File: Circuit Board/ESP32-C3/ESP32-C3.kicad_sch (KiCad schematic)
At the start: 41 parts

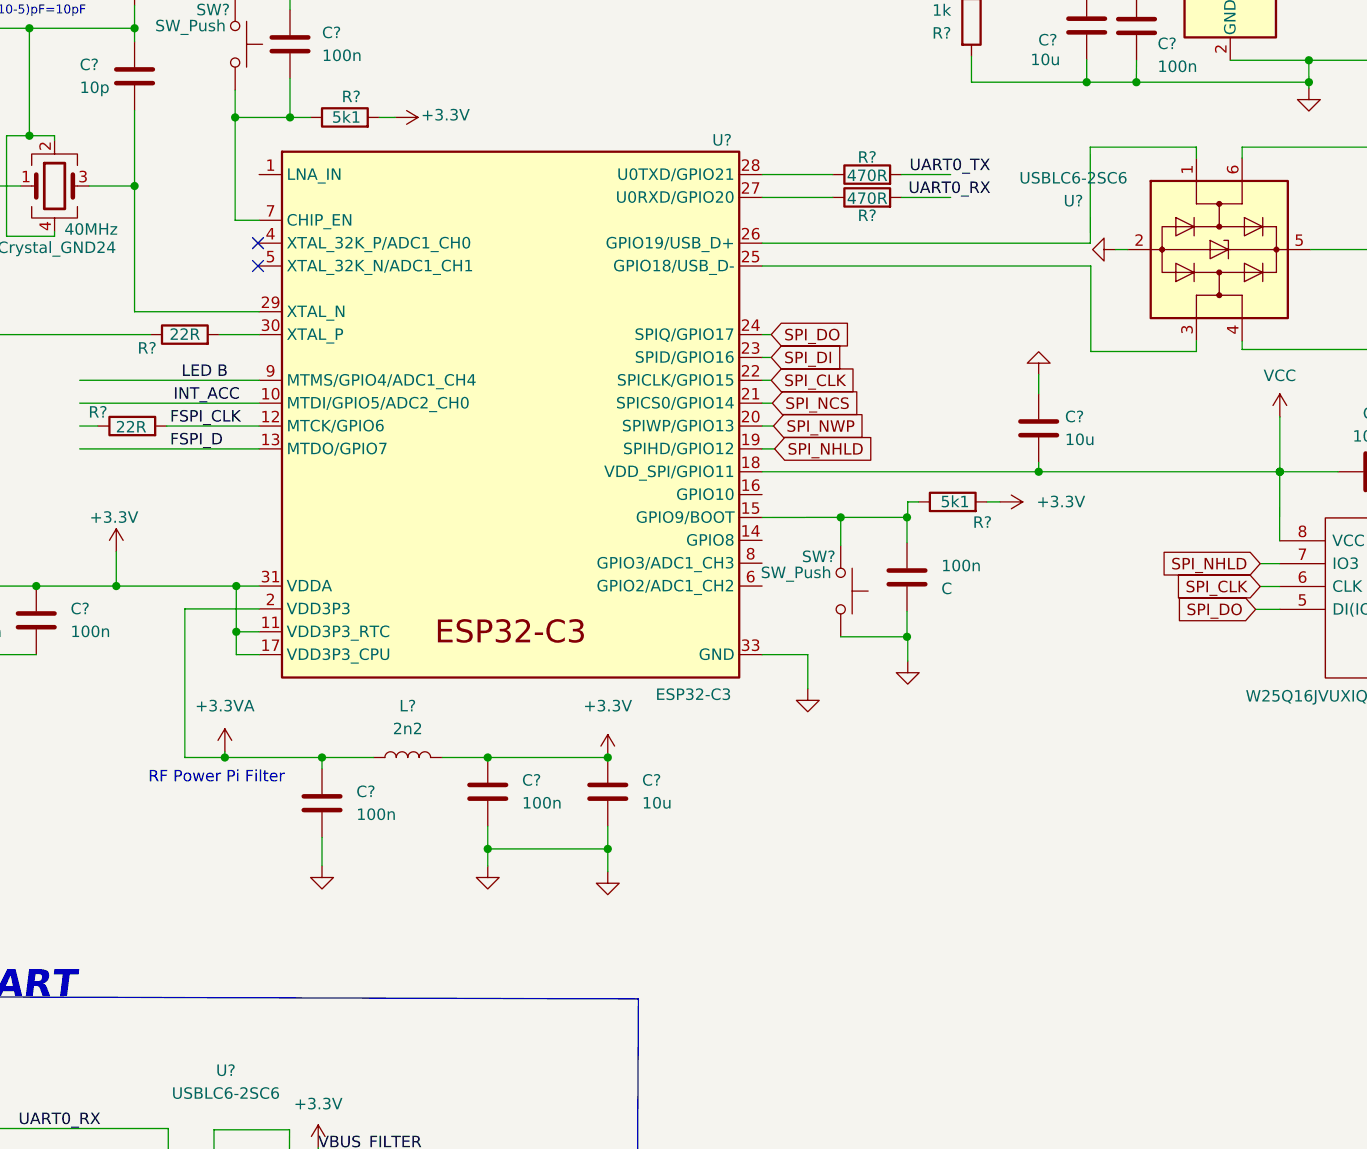
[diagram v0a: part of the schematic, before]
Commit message: Added RF antenna circuit
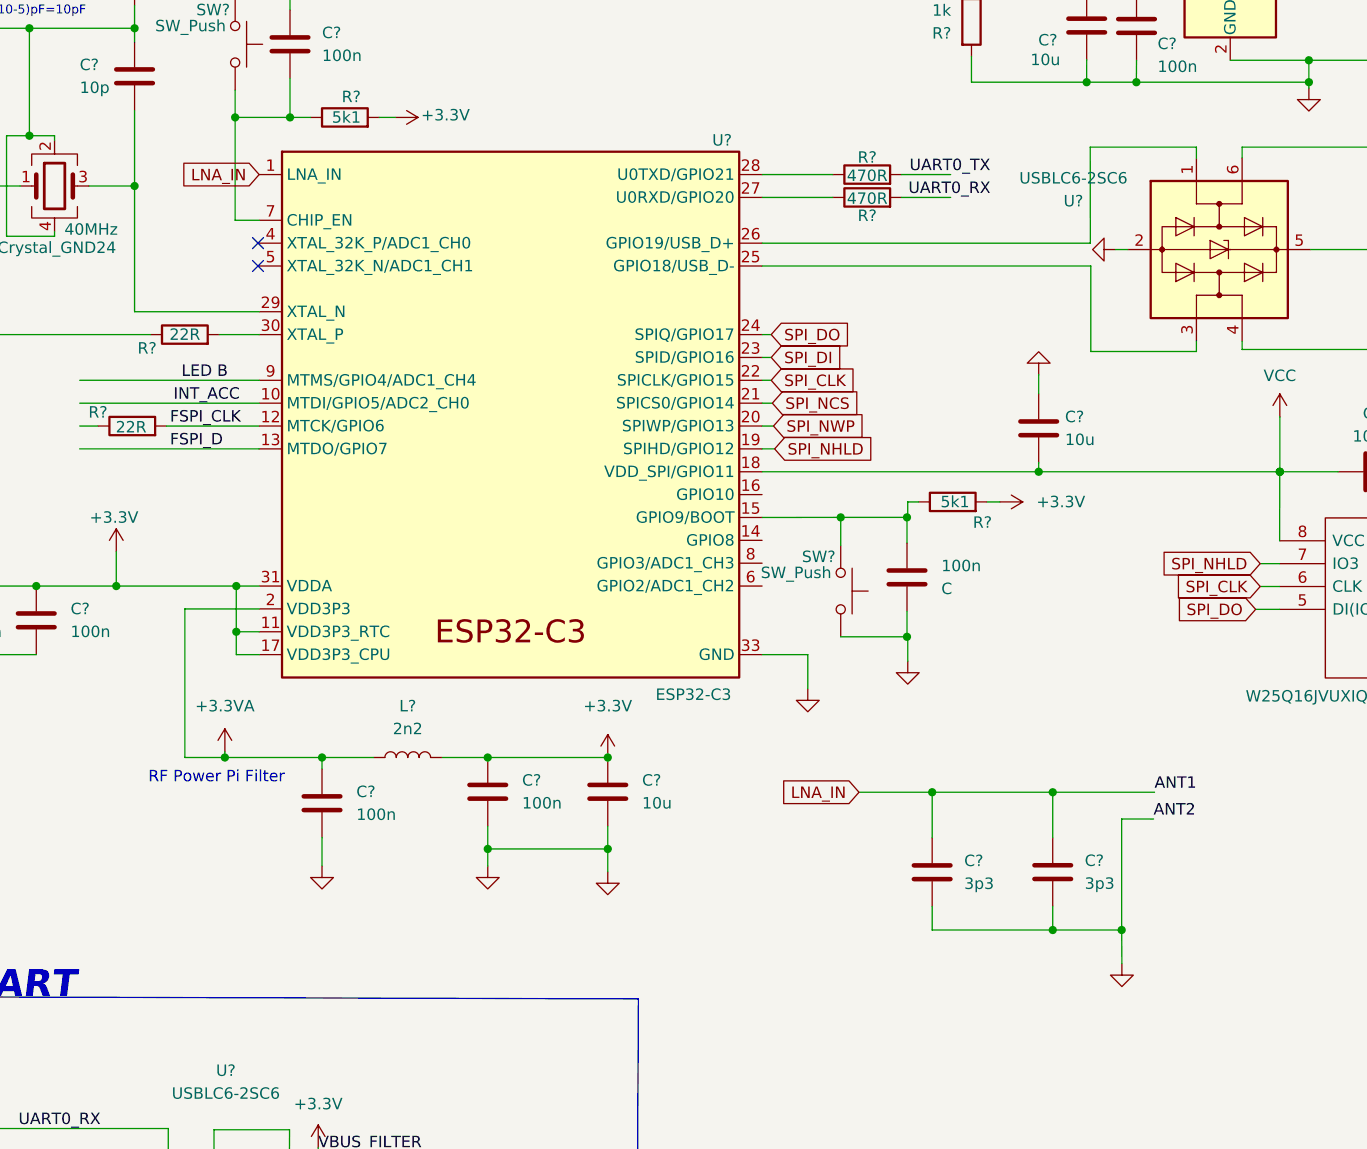
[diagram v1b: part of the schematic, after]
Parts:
- added C? (x2): 3p3, symbol Device:C
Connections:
- net +3.3V: now also C?.2, C?.2
- net LNA_IN: now reaches U?.1 (LNA_IN)
- net LNA_IN: now also C?.1, C?.1
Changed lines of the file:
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@@
   (junction (at 119.1514 120.5992) (diameter 0) (color 0 0 0 0)
   )
+  (junction (at 155.194 114.3) (diameter 0) (color 0 0 0 0)
+  )
   (junction (at 77.8764 96.4692) (diameter 0) (color 0 0 0 0)
   )
+  (junction (at 168.5923 114.2998) (diameter 0) (color 0 0 0 0)
+  )
   (junction (at 193.8274 78.6892) (diameter 0) (color 0 0 0 0)
   )
@@
   (junction (at 77.8764 91.3892) (diameter 0) (color 0 0 0 0)
   )
+  (junction (at 176.2524 129.6082) (diameter 0) (color 0 0 0 0)
+  )
   (junction (at 87.4014 110.4392) (diameter 0) (color 0 0 0 0)
   )
@@
   )
   (junction (at 145.034 83.7593) (diameter 0) (color 0 0 0 0)
+  )
+  (junction (at 168.5923 129.6082) (diameter 0) (color 0 0 0 0)
   )
   (junction (at 177.8846 35.4076) (diameter 0) (color 0 0 0 0)
@@
     (stroke (width 0) (type default) (color 0 0 0 0))
   )
+  (wire (pts (xy 155.194 127) (xy 155.194 129.6082))
+    (stroke (width 0) (type default) (color 0 0 0 0))
+  )
   (wire (pts (xy 75.3991 154.044) (xy 75.3991 151.802))
     (stroke (width 0) (type default) (color 0 0 0 0))
@@
     (stroke (width 0) (type default) (color 0 0 0 0))
   )
+  (wire (pts (xy 168.5923 114.2998) (xy 168.5923 119.3656))
+    (stroke (width 0) (type default) (color 0 0 0 0))
+  )
   (wire (pts (xy 159.5628 22.8057) (xy 159.5628 24.892))
     (stroke (width 0) (type default) (color 0 0 0 0))
@@
     (stroke (width 0) (type default) (color 0 0 0 0))
   )
+  (wire (pts (xy 147.066 114.3) (xy 155.194 114.3))
+    (stroke (width 0) (type default) (color 0 0 0 0))
+  )
   (wire (pts (xy 152.484 97.028) (xy 152.484 99.748))
     (stroke (width 0) (type default) (color 0 0 0 0))
@@
     (stroke (width 0) (type default) (color 0 0 0 0))
   )
+  (wire (pts (xy 155.194 114.3) (xy 168.5923 114.2998))
+    (stroke (width 0) (type default) (color 0 0 0 0))
+  )
   (wire (pts (xy 255.8542 77.3684) (xy 255.8796 73.4568))
     (stroke (width 0) (type default) (color 0 0 0 0))
@@
     (stroke (width 0) (type default) (color 0 0 0 0))
   )
+  (wire (pts (xy 168.5923 129.6082) (xy 176.2524 129.6082))
+    (stroke (width 0) (type default) (color 0 0 0 0))
+  )
   (wire (pts (xy 66.5734 46.9392) (xy 66.5734 60.9092))
     (stroke (width 0) (type default) (color 0 0 0 0))
@@
     (stroke (width 0) (type default) (color 0 0 0 0))
   )
+  (wire (pts (xy 168.5923 129.6082) (xy 168.5923 126.9856))
+    (stroke (width 0) (type default) (color 0 0 0 0))
+  )
+  (wire (pts (xy 155.194 114.3) (xy 155.194 119.38))
+    (stroke (width 0) (type default) (color 0 0 0 0))
+  )
   (wire (pts (xy 75.3991 174.364) (xy 75.3991 177.0155))
     (stroke (width 0) (type default) (color 0 0 0 0))
@@
     (stroke (width 0) (type default) (color 0 0 0 0))
   )
+  (wire (pts (xy 176.2524 117.2715) (xy 179.7925 117.2763))
+    (stroke (width 0) (type default) (color 0 0 0 0))
+  )
   (wire (pts (xy 45.7454 30.6832) (xy 45.7454 29.4132))
     (stroke (width 0) (type default) (color 0 0 0 0))
@@
     (stroke (width 0) (type default) (color 0 0 0 0))
   )
+  (wire (pts (xy 176.2524 129.6082) (xy 176.2524 117.2715))
+    (stroke (width 0) (type default) (color 0 0 0 0))
+  )
   (wire (pts (xy 167.0304 78.6892) (xy 167.0304 77.6732))
     (stroke (width 0) (type default) (color 0 0 0 0))
@@
     (stroke (width 0) (type default) (color 0 0 0 0))
   )
+  (wire (pts (xy 168.5923 114.2998) (xy 179.9008 114.2998))
+    (stroke (width 0) (type default) (color 0 0 0 0))
+  )
   (wire (pts (xy 223.6216 40.4368) (xy 218.4633 40.4368))
     (stroke (width 0) (type default) (color 0 0 0 0))
@@
     (stroke (width 0) (type default) (color 0 0 0 0))
   )
+  (wire (pts (xy 176.276 133.35) (xy 176.2524 129.6082))
+    (stroke (width 0) (type default) (color 0 0 0 0))
+  )
   (wire (pts (xy 197.998 22.8092) (xy 206.248 22.8092))
+    (stroke (width 0) (type default) (color 0 0 0 0))
+  )
+  (wire (pts (xy 155.194 129.6082) (xy 168.5923 129.6082))
     (stroke (width 0) (type default) (color 0 0 0 0))
   )
@@
     (effects (font (size 1 1)) (justify left bottom))
   )
+  (label "ANT1" (at 179.9008 114.2998 0)
+    (effects (font (size 1.27 1.27)) (justify left bottom))
+  )
   (label "LED B" (at 71.7804 68.5292 0)
     (effects (font (size 1.27 1.27)) (justify left bottom))
@@
   )
   (label "VBUS_FILTER" (at 86.9797 154.2376 0)
+    (effects (font (size 1.27 1.27)) (justify left bottom))
+  )
+  (label "ANT2" (at 179.7925 117.2763 0)
     (effects (font (size 1.27 1.27)) (justify left bottom))
   )
@@
     (effects (font (size 1.27 1.27)) (justify right))
     (property "Intersheet References" "${INTERSHEET_REFS}" (id 0) (at 181.6099 91.3606 0)
+      (effects (font (size 1.27 1.27)) (justify right) hide)
+    )
+  )
+  (global_label "LNA_IN" (shape input) (at 80.4164 45.6692 180) (fields_autoplaced)
+    (effects (font (size 1.27 1.27)) (justify right))
+    (property "Intersheet References" "${INTERSHEET_REFS}" (id 0) (at 71.6533 45.5898 0)
+      (effects (font (size 1.27 1.27)) (justify right) hide)
+    )
+  )
+  (global_label "LNA_IN" (shape input) (at 147.066 114.3 180) (fields_autoplaced)
+    (effects (font (size 1.27 1.27)) (justify right))
+    (property "Intersheet References" "${INTERSHEET_REFS}" (id 0) (at 138.3029 114.2206 0)
       (effects (font (size 1.27 1.27)) (justify right) hide)
     )
@@
     (pin "2")
   )
+  (symbol (lib_id "Device:C") (at 155.194 123.19 0) (unit 1)
+    (in_bom yes) (on_board yes) (fields_autoplaced)
+    (property "Reference" "C?" (id 0) (at 158.75 121.9199 0)
+      (effects (font (size 1.27 1.27)) (justify left))
+    )
+    (property "Value" "3p3" (id 1) (at 158.75 124.4599 0)
+      (effects (font (size 1.27 1.27)) (justify left))
+    )
+    (property "Footprint" "" (id 2) (at 156.1592 127 0)
+      (effects (font (size 1.27 1.27)) hide)
+    )
+    (property "Datasheet" "~" (id 3) (at 155.194 123.19 0)
+      (effects (font (size 1.27 1.27)) hide)
+    )
+    (pin "1")
+    (pin "2")
+  )
   (symbol (lib_id "Device:C") (at 216.8652 26.6192 0) (unit 1)
     (in_bom yes) (on_board yes) (fields_autoplaced)
@@
     (pin "2")
   )
+  (symbol (lib_id "power:GND") (at 176.276 133.35 0) (unit 1)
+    (in_bom yes) (on_board yes) (fields_autoplaced)
+    (property "Reference" "#PWR?" (id 0) (at 176.276 139.7 0)
+      (effects (font (size 1.27 1.27)) hide)
+    )
+    (property "Value" "GND" (id 1) (at 176.276 138.43 0)
+      (effects (font (size 1.27 1.27)) hide)
+    )
+    (property "Footprint" "" (id 2) (at 176.276 133.35 0)
+      (effects (font (size 1.27 1.27)) hide)
+    )
+    (property "Datasheet" "" (id 3) (at 176.276 133.35 0)
+      (effects (font (size 1.27 1.27)) hide)
+    )
+    (pin "1")
+  )
   (symbol (lib_id "power:GND") (at 255.8542 77.3684 0) (mirror y) (unit 1)
     (in_bom yes) (on_board yes) (fields_autoplaced)
@@
     )
     (property "Datasheet" "~" (id 3) (at 152.4 90.424 0)
+      (effects (font (size 1.27 1.27)) hide)
+    )
+    (pin "1")
+    (pin "2")
+  )
+  (symbol (lib_id "Device:C") (at 168.5923 123.1756 0) (unit 1)
+    (in_bom yes) (on_board yes) (fields_autoplaced)
+    (property "Reference" "C?" (id 0) (at 172.1483 121.9055 0)
+      (effects (font (size 1.27 1.27)) (justify left))
+    )
+    (property "Value" "3p3" (id 1) (at 172.1483 124.4455 0)
+      (effects (font (size 1.27 1.27)) (justify left))
+    )
+    (property "Footprint" "" (id 2) (at 169.5575 126.9856 0)
+      (effects (font (size 1.27 1.27)) hide)
+    )
+    (property "Datasheet" "~" (id 3) (at 168.5923 123.1756 0)
       (effects (font (size 1.27 1.27)) hide)
     )
@@
       (reference "#PWR?") (unit 1) (value "+3.3V") (footprint "")
     )
+    (path "/d98751d6-ec4f-464b-80dc-6563757d270e"
+      (reference "#PWR?") (unit 1) (value "GND") (footprint "")
+    )
     (path "/df767990-b364-4910-9641-a5baaff2e52a"
       (reference "#PWR?") (unit 1) (value "GND") (footprint "")
@@
       (reference "C?") (unit 1) (value "100n") (footprint "")
     )
+    (path "/532788d1-7b03-4a7b-8338-1b2626ce6f82"
+      (reference "C?") (unit 1) (value "3p3") (footprint "")
+    )
     (path "/61680386-e495-4323-b942-055dd2da6292"
       (reference "C?") (unit 1) (value "100n") (footprint "")
@@
       (reference "C?") (unit 1) (value "100n") (footprint "")
     )
+    (path "/f1acd559-10d6-43fd-85f8-ccf95d71c1da"
+      (reference "C?") (unit 1) (value "3p3") (footprint "")
+    )
     (path "/f320bd8c-186a-4319-ac4d-7c794071fbbd"

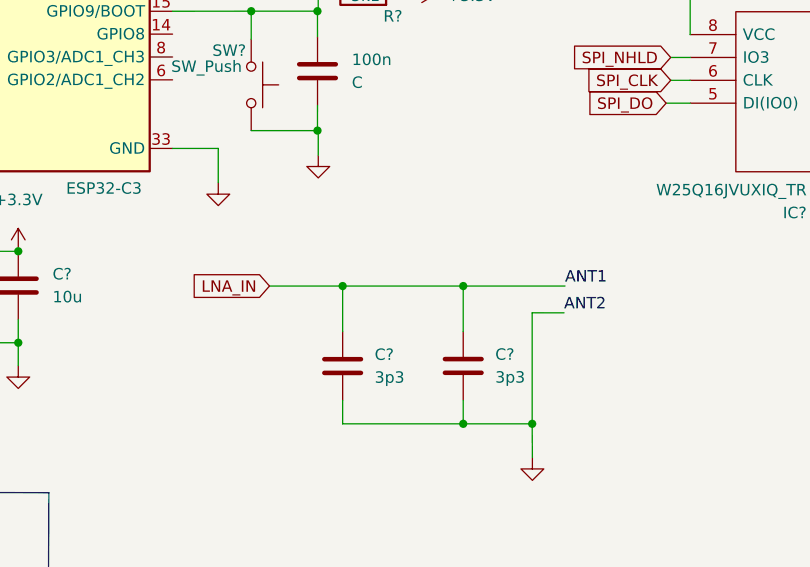
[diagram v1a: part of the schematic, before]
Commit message: Added RF antenna inductor
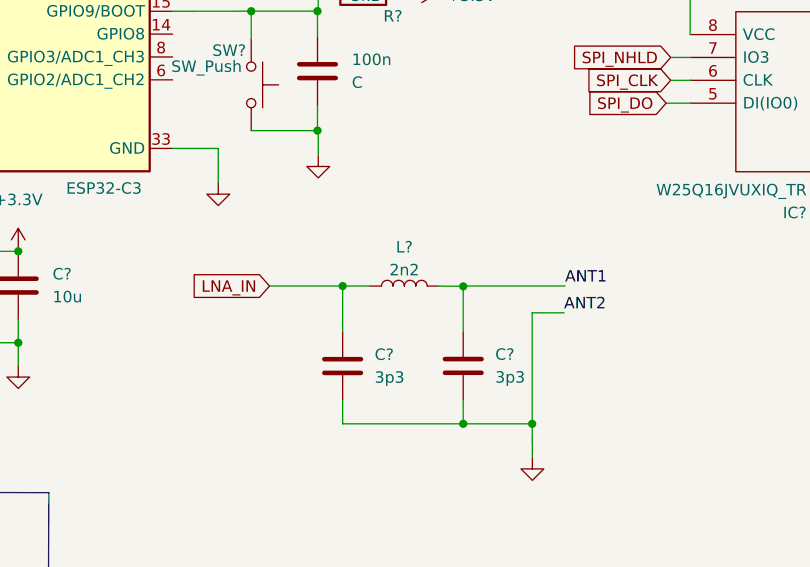
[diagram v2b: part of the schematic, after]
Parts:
- added L?: 2n2, symbol Device:L
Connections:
- net LNA_IN: now also L?.1; no longer C?.1
- new net ANT1: C?.1, L?.2
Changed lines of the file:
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@@
   (junction (at 119.1514 120.5992) (diameter 0) (color 0 0 0 0)
   )
+  (junction (at 168.5923 114.3333) (diameter 0) (color 0 0 0 0)
+  )
+  (junction (at 77.8764 96.4692) (diameter 0) (color 0 0 0 0)
+  )
+  (junction (at 193.8274 78.6892) (diameter 0) (color 0 0 0 0)
+  )
+  (junction (at 152.3963 97.028) (diameter 0) (color 0 0 0 0)
+  )
+  (junction (at 197.0513 32.9692) (diameter 0) (color 0 0 0 0)
+  )
+  (junction (at 167.0304 78.6892) (diameter 0) (color 0 0 0 0)
+  )
+  (junction (at 170.7856 22.8092) (diameter 0) (color 0 0 0 0)
+  )
+  (junction (at 193.8155 78.6892) (diameter 0) (color 0 0 0 0)
+  )
+  (junction (at 83.8454 39.3192) (diameter 0) (color 0 0 0 0)
+  )
+  (junction (at 216.8652 22.8092) (diameter 0) (color 0 0 0 0)
+  )
+  (junction (at 54.8894 29.4132) (diameter 0) (color 0 0 0 0)
+  )
+  (junction (at 20.7264 99.0092) (diameter 0) (color 0 0 0 0)
+  )
+  (junction (at 32.1564 99.0092) (diameter 0) (color 0 0 0 0)
+  )
+  (junction (at 234.1372 35.3411) (diameter 0) (color 0 0 0 0)
+  )
   (junction (at 155.194 114.3) (diameter 0) (color 0 0 0 0)
-  )
-  (junction (at 77.8764 96.4692) (diameter 0) (color 0 0 0 0)
-  )
-  (junction (at 168.5923 114.2998) (diameter 0) (color 0 0 0 0)
-  )
-  (junction (at 193.8274 78.6892) (diameter 0) (color 0 0 0 0)
-  )
-  (junction (at 152.3963 97.028) (diameter 0) (color 0 0 0 0)
-  )
-  (junction (at 197.0513 32.9692) (diameter 0) (color 0 0 0 0)
-  )
-  (junction (at 167.0304 78.6892) (diameter 0) (color 0 0 0 0)
-  )
-  (junction (at 170.7856 22.8092) (diameter 0) (color 0 0 0 0)
-  )
-  (junction (at 193.8155 78.6892) (diameter 0) (color 0 0 0 0)
-  )
-  (junction (at 83.8454 39.3192) (diameter 0) (color 0 0 0 0)
-  )
-  (junction (at 216.8652 22.8092) (diameter 0) (color 0 0 0 0)
-  )
-  (junction (at 54.8894 29.4132) (diameter 0) (color 0 0 0 0)
-  )
-  (junction (at 20.7264 99.0092) (diameter 0) (color 0 0 0 0)
-  )
-  (junction (at 32.1564 99.0092) (diameter 0) (color 0 0 0 0)
-  )
-  (junction (at 234.1372 35.3411) (diameter 0) (color 0 0 0 0)
   )
   (junction (at 66.5734 46.9392) (diameter 0) (color 0 0 0 0)
@@
     (stroke (width 0) (type default) (color 0 0 0 0))
   )
+  (wire (pts (xy 155.194 114.3) (xy 158.242 114.3))
+    (stroke (width 0) (type default) (color 0 0 0 0))
+  )
   (wire (pts (xy 83.7939 151.802) (xy 83.7586 160.2415))
     (stroke (width 0) (type default) (color 0 0 0 0))
@@
     (stroke (width 0) (type default) (color 0 0 0 0))
   )
-  (wire (pts (xy 168.5923 114.2998) (xy 168.5923 119.3656))
+  (wire (pts (xy 168.5923 114.2998) (xy 168.5923 114.3333))
     (stroke (width 0) (type default) (color 0 0 0 0))
   )
@@
     (stroke (width 0) (type default) (color 0 0 0 0))
   )
-  (wire (pts (xy 155.194 114.3) (xy 168.5923 114.2998))
-    (stroke (width 0) (type default) (color 0 0 0 0))
-  )
   (wire (pts (xy 255.8542 77.3684) (xy 255.8796 73.4568))
     (stroke (width 0) (type default) (color 0 0 0 0))
@@
     (stroke (width 0) (type default) (color 0 0 0 0))
   )
+  (wire (pts (xy 165.862 114.3) (xy 168.5923 114.3333))
+    (stroke (width 0) (type default) (color 0 0 0 0))
+  )
   (wire (pts (xy 137.3124 68.5292) (xy 136.2964 68.5292))
     (stroke (width 0) (type default) (color 0 0 0 0))
@@
   )
   (wire (pts (xy 76.6064 110.4392) (xy 76.6064 109.8042))
+    (stroke (width 0) (type default) (color 0 0 0 0))
+  )
+  (wire (pts (xy 168.5923 114.3333) (xy 168.5923 119.3656))
     (stroke (width 0) (type default) (color 0 0 0 0))
   )
@@
     (pin "1")
   )
+  (symbol (lib_id "Device:L") (at 162.052 114.3 90) (unit 1)
+    (in_bom yes) (on_board yes)
+    (property "Reference" "L?" (id 0) (at 162.052 109.982 90))
+    (property "Value" "2n2" (id 1) (at 162.052 112.522 90))
+    (property "Footprint" "" (id 2) (at 162.052 114.3 0)
+      (effects (font (size 1.27 1.27)) hide)
+    )
+    (property "Datasheet" "~" (id 3) (at 162.052 114.3 0)
+      (effects (font (size 1.27 1.27)) hide)
+    )
+    (pin "1")
+    (pin "2")
+  )
   (symbol (lib_id "Device:C") (at 66.5734 34.7472 0) (unit 1)
     (in_bom yes) (on_board yes)
@@
       (reference "L?") (unit 1) (value "2n2") (footprint "")
     )
+    (path "/c8fb7657-ab0f-4909-b68f-eca4047360e4"
+      (reference "L?") (unit 1) (value "2n2") (footprint "")
+    )
